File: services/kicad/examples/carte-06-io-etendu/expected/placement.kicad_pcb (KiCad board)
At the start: 2 copper layers, 80 x 60 mm, 35 parts, among them J1 IN_5V, J10 IO0, J11 IO1, J2 SWD, U1 STM32F103C8T6, U2 AMS1117-3.3

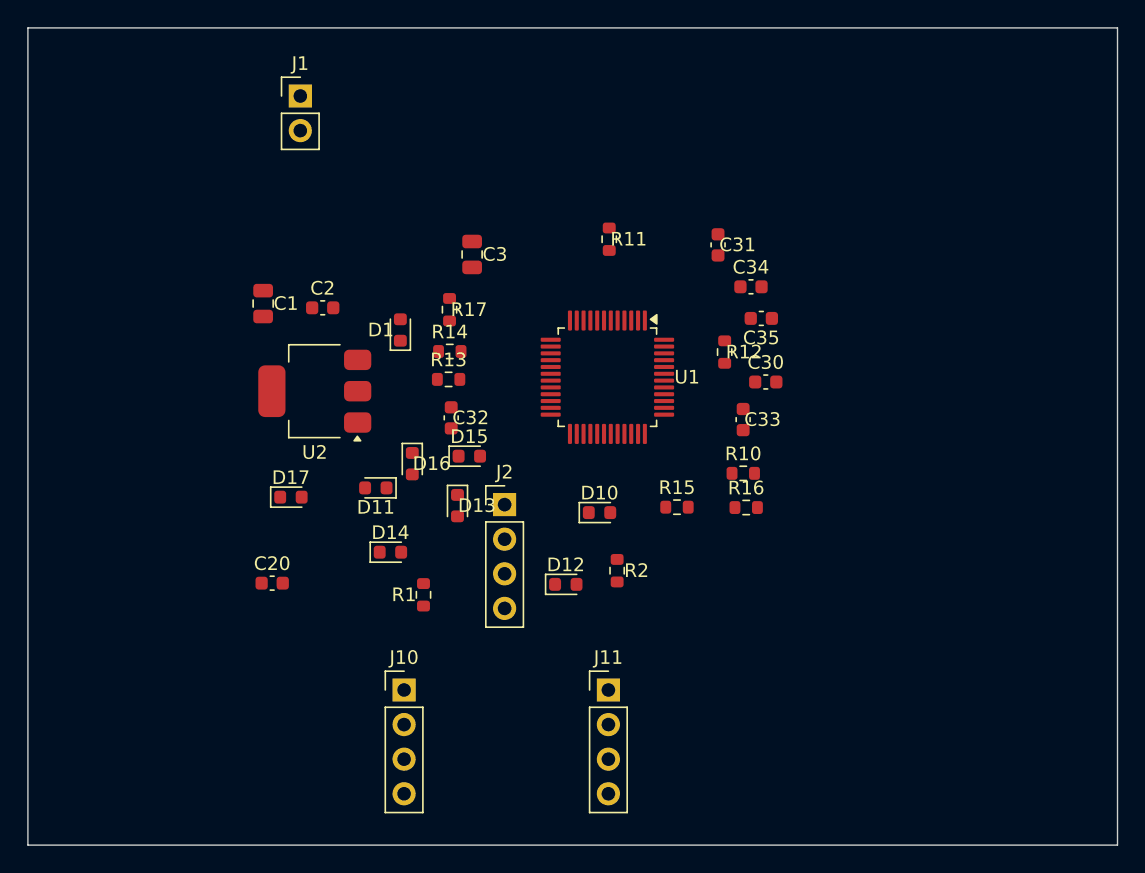
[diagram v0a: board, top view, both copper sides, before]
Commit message: fix(routing): GND route par defaut, plan sur reglage -- sites et tests alignes
Quatre sites de routing.py lisaient encore `_nets_confies_au_plan()` au
lieu de la constante `_NETS_CONFIES_AU_PLAN` que le module reaffecte et que
les tests remplacent : le reglage n atteignait pas ces sites. L escalade
n avait plus de repli vers `_NETS_DE_PLAN_CONNUS` (une connexion GND
manquante doit pouvoir escalader quand GND est route).

Tests encodant l ancienne strategie (GND confie au plan) recrits : les deux
cas sont couverts, GND route par defaut (decision utilisateur du 2026-09-10,
reference STM32 Astra + docs/methodologie-routage.md) et GND confie au plan
sur le reglage `gnd_confie_au_plan`.

`_reattribuer_les_decouplages` rend intact ce qui n est pas une liste.
Deux tests de journal Freerouting comparaient un chemin Windows a un
entrypoint POSIX : `as_posix()`.

Cartes 01, 02, 03, 04, 06 regenerees avec GND route : 100 % routees,
0 erreur DRC, fabricables ; placement.kicad_pcb livre pour chacune.

1630 passed, 2 skipped.

Co-Authored-By: Claude Fable 5.1 <noreply@anthropic.com>
Claude-Session: https://claude.ai/code/session_01TnMqm4La2CxQHHB5K8aSSV
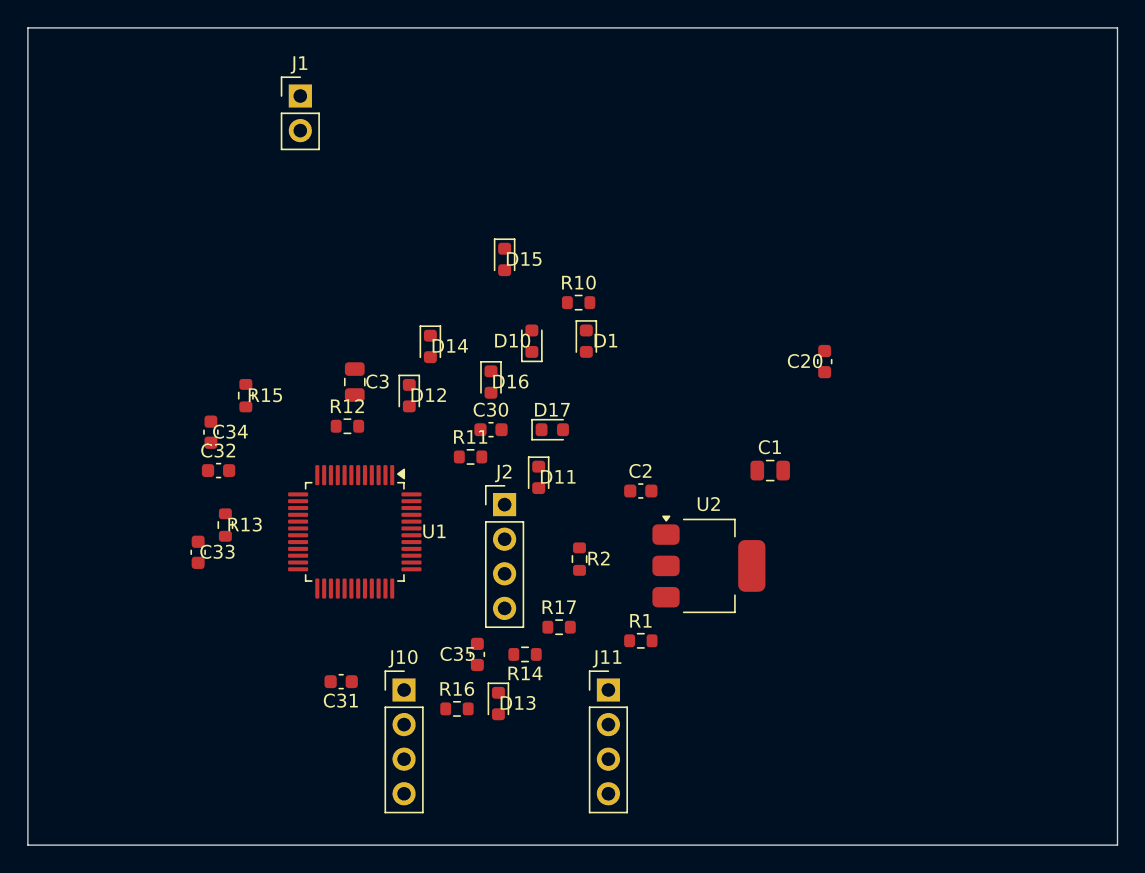
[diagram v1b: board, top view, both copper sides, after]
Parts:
- moved C20 43.7 mm to (167.0, 99.5), turned to 90 degrees
- moved C31 42.4 mm to (131.5, 123.0), turned to 180 degrees
- moved C33 41.2 mm to (121.0, 113.5)
- moved C34 41.1 mm to (121.9, 104.7), turned to 270 degrees
- moved C1 39.2 mm to (163.0, 107.5), turned to 0 degrees
- moved R15 32.7 mm to (124.5, 102.0), turned to 270 degrees
- moved C35 32.3 mm to (141.5, 121.0), turned to 90 degrees
- moved U2 31.7 mm to (158.5, 114.5), turned to 0 degrees
- moved R12 28.2 mm to (132.0, 104.2), turned to 0 degrees
- moved C2 27.0 mm to (153.5, 109.0)
- moved R16 25.9 mm to (140.0, 125.0)
- moved R17 24.7 mm to (147.5, 119.0), turned to 0 degrees
- moved R14 22.9 mm to (145.0, 121.0), turned to 180 degrees
- moved U1 21.7 mm to (132.5, 112.0)
- moved C30 20.5 mm to (142.5, 104.5)
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
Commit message: examples: carte-01 a 07 -- placement valide et gele (phase 1) puis route dessus (phase 2) : 100 %, 0 erreur, 2 couches
Sequence en deux phases demandee par l'utilisateur : valider_placements.py (critere pro : chaque broche VDD a sa capa a <= 3,5 mm) puis banc_exemples.py --placement-fige. 30 s a 2,6 min de routage par carte.

Co-Authored-By: Claude Fable 5.1 <noreply@anthropic.com>

Claude-Session: https://claude.ai/code/session_01TnMqm4La2CxQHHB5K8aSSV
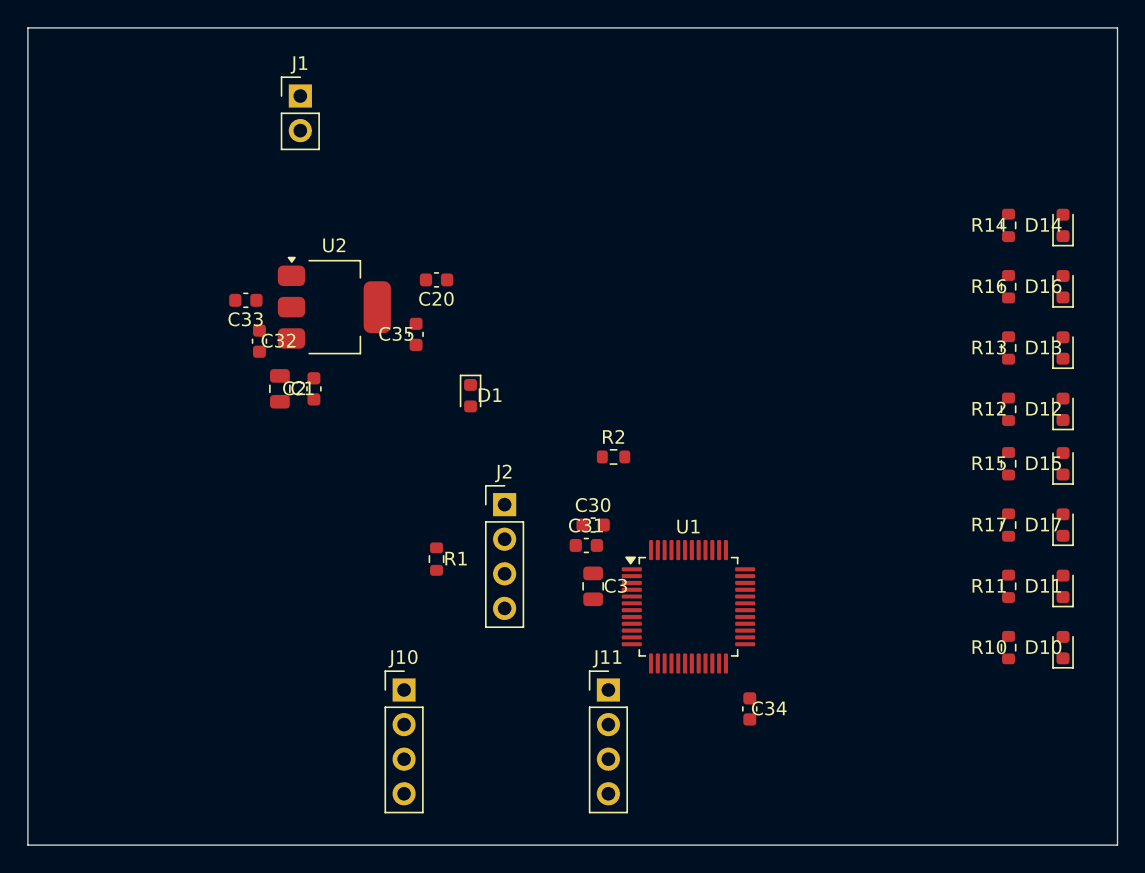
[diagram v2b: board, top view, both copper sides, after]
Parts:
- moved R13 59.0 mm to (180.5, 98.5), turned to 90 degrees
- moved R15 56.2 mm to (180.5, 107.0), turned to 90 degrees
- moved R16 51.0 mm to (180.5, 94.0), turned to 90 degrees
- moved D13 49.0 mm to (184.5, 98.5), turned to 90 degrees
- moved R12 48.6 mm to (180.5, 103.0), turned to 90 degrees
- moved D12 48.0 mm to (184.5, 103.0), turned to 90 degrees
- moved R14 47.5 mm to (180.5, 89.5), turned to 90 degrees
- moved D14 47.3 mm to (184.5, 89.5), turned to 90 degrees
- moved D10 45.0 mm to (184.5, 120.5)
- moved C34 44.5 mm to (161.5, 125.0)
- moved D15 43.7 mm to (184.5, 107.0), turned to 90 degrees
- moved D16 42.6 mm to (184.5, 94.0), turned to 90 degrees
- moved R11 40.6 mm to (180.5, 116.0), turned to 90 degrees
- moved R10 40.5 mm to (180.5, 120.5), turned to 90 degrees
- moved D11 39.3 mm to (184.5, 116.0), turned to 90 degrees
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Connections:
- U1 pad 36: +3V3 -> Net-(U1-36)
- U1 pad 48: +3V3 -> Net-(U1-48)
